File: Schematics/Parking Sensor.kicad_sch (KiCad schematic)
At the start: 7 parts, among them M1 U?, SW1 SW_Push, U1 VL53L1X_Board, U2 WS2812

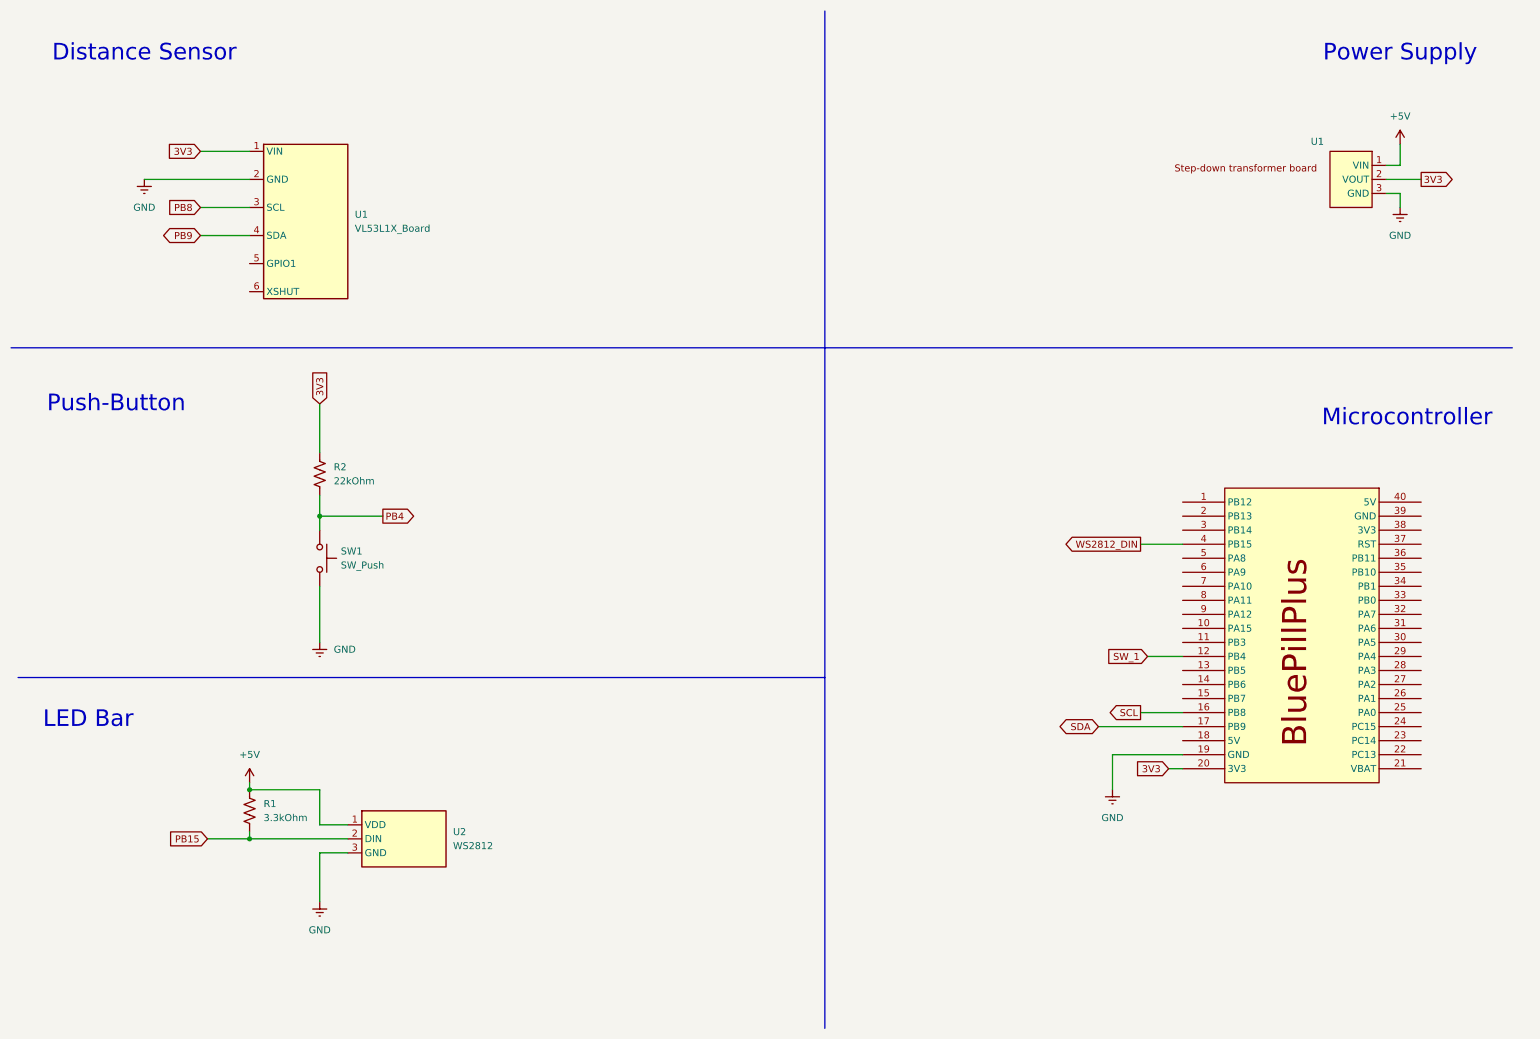
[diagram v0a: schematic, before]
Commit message: Updated schematics adding LIDAR interrupt and MOSFET to control LED bar power
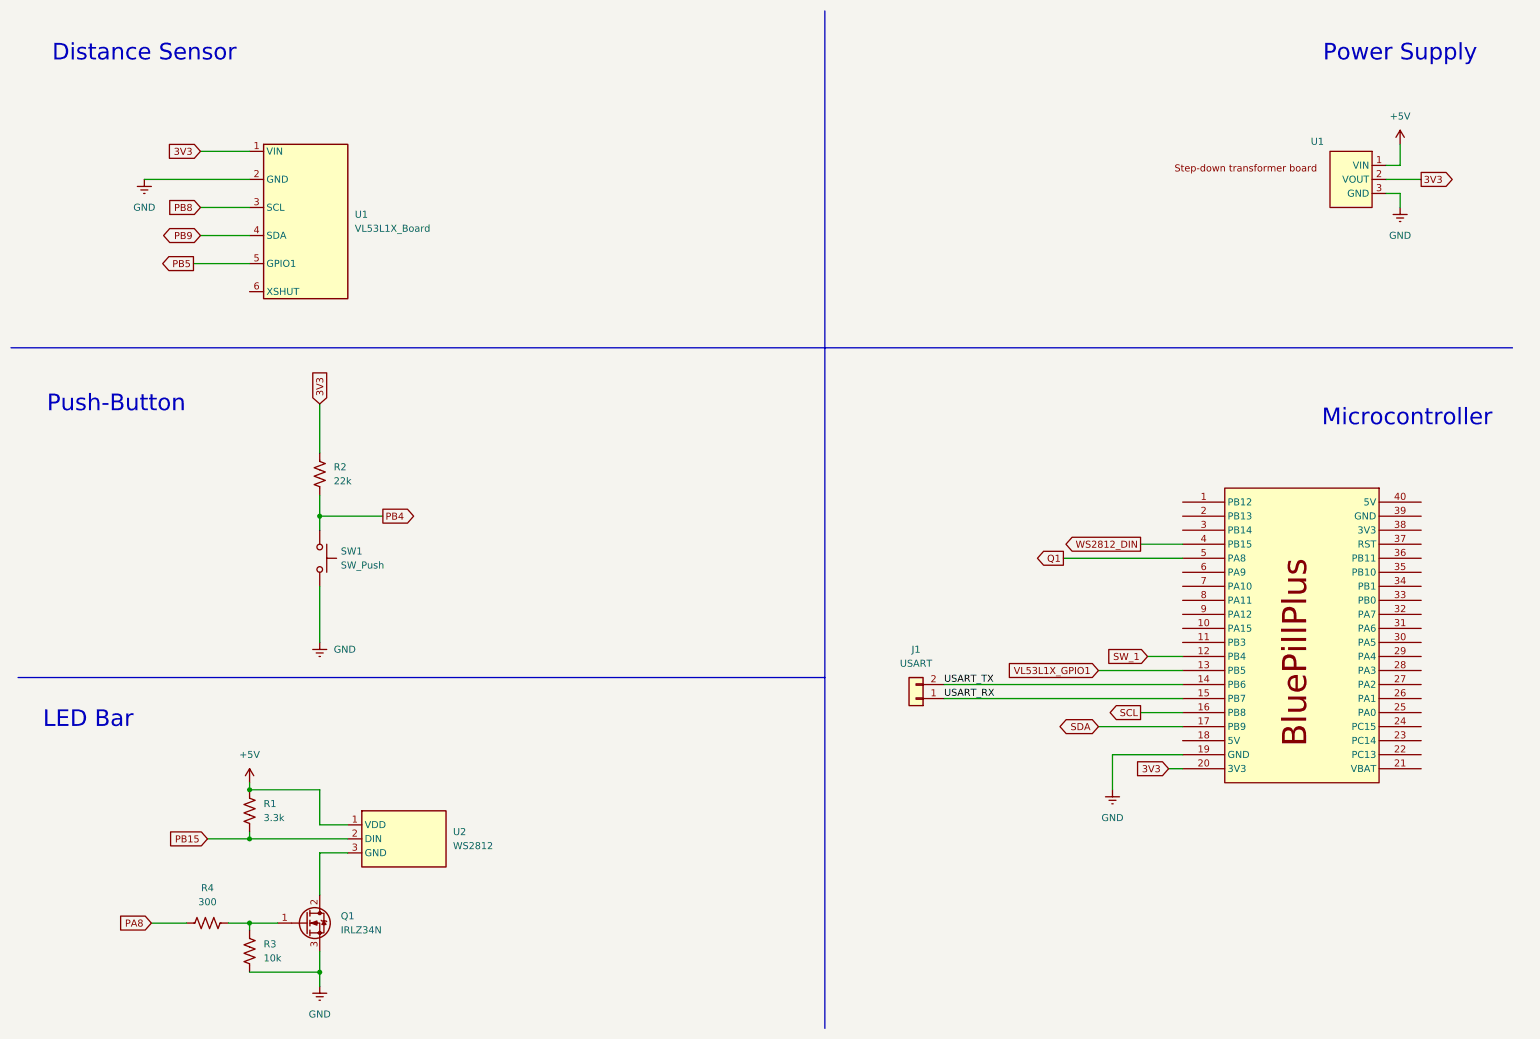
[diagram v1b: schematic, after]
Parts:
- added J1: USART, symbol Connector_Generic:Conn_01x02
- added Q1: IRLZ34N, Package_TO_SOT_THT:TO-220-3_Vertical, symbol Transistor_FET:IRLZ34N
- added R3: 10k, symbol Device:R_US
- added R4: 300, symbol Device:R_US
- R1: value 3.3kOhm -> 3.3k
- R2: value 22kOhm -> 22k
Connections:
- net GND: now also Q1.3 (S), R3.2; no longer U2.3 (GND)
- net PB5: now reaches U1.5 (GPIO1)
- net VL53L1X_GPIO1: now reaches M1.13 (PB5)
- net USART_TX: now reaches M1.14 (PB6)
- net USART_TX: now also J1.2 (Pin_2)
- net USART_RX: now reaches M1.15 (PB7)
- net USART_RX: now also J1.1 (Pin_1)
- net Q1: now reaches M1.5 (PA8)
- new net: Q1.1 (G), R3.1, R4.2
- new net: Q1.2 (D), U2.3 (GND)
- new net PA8: R4.1
